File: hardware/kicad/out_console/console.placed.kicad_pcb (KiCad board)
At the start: 2 copper layers, 99.5 x 99.5 mm, 65 parts, among them J1 RaspberryPi_Pico_SMD_HandSold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, J10 JST_XH_B2B-XH-A_1x02_P2.50mm_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, J11 JST_XH_B2B-XH-A_1x02_P2.50mm_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, J12 JST_XH_B2B-XH-A_1x02_P2.50mm_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, J13 JST_XH_B2B-XH-A_1x02_P2.50mm_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, J14 JST_XH_B2B-XH-A_1x02_P2.50mm_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, J15 JST_XH_B2B-XH-A_1x02_P2.50mm_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, J16 JST_XH_B2B-XH-A_1x02_P2.50mm_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, J17 JST_XH_B2B-XH-A_1x02_P2.50mm_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, J18 JST_XH_B2B-XH-A_1x02_P2.50mm_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, J19 JST_XH_B2B-XH-A_1x02_P2.50mm_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, J2 IDC-Header_2x20_P2.54mm_Verti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, J20 JST_XH_B4B-XH-A_1x04_P2.50mm_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, J21 JST_XH_B4B-XH-A_1x04_P2.50mm_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, J22 PinHeader_2x03_P2.54mm_Vertic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, J23 JST_XH_B3B-XH-A_1x03_P2.50mm_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, J24 JST_VH_B3P-VH_1x03_P3.96mm_Ve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, J3 JST_VH_B2P-VH_1x02_P3.96mm_Ve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, J4 JST_XH_B3B-XH-A_1x03_P2.50mm_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, J5 JST_XH_B2B-XH-A_1x02_P2.50mm_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, J6 JST_XH_B4B-XH-A_1x04_P2.50mm_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, J8 JST_XH_B2B-XH-A_1x02_P2.50mm_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, J9 JST_XH_B2B-XH-A_1x02_P2.50mm_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, U1 DIP-14_W7.62mm, U2 DIP-6_W7.62mm

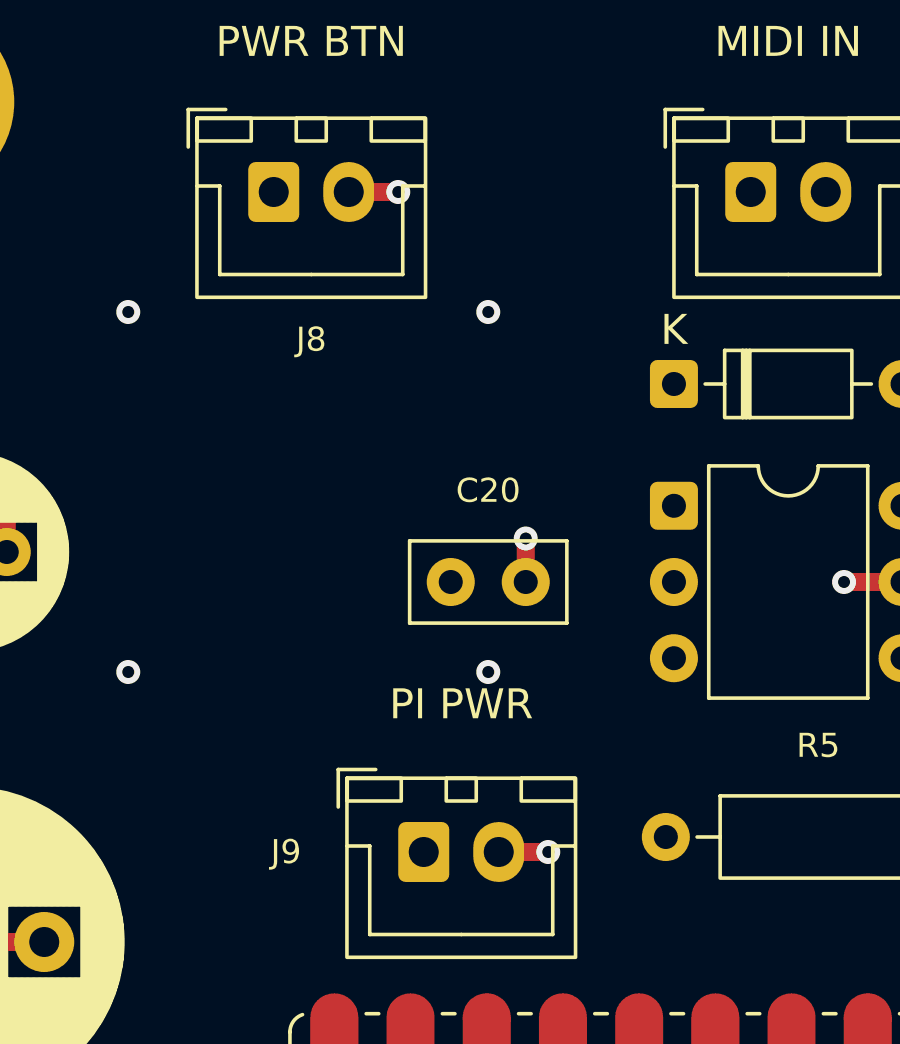
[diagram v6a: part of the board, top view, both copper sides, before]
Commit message: fix(hardware): the power button lead is a floating pair, not signal and GND (#1062)
J8 and J9 were wired PWR_BTN + GND. Nothing on the board reads the button,
and a lead fitted to the Pi 5's J2 pads the wrong way round held the button
pad at ground, which the Pi reads as a button held down. They are now wired
pin to pin (PWR_BTN, PWR_BTN_RET) with neither touching GND, so the lead
works either way round. PWR_BTN gates the floating pair; rerouted, DRC clean.
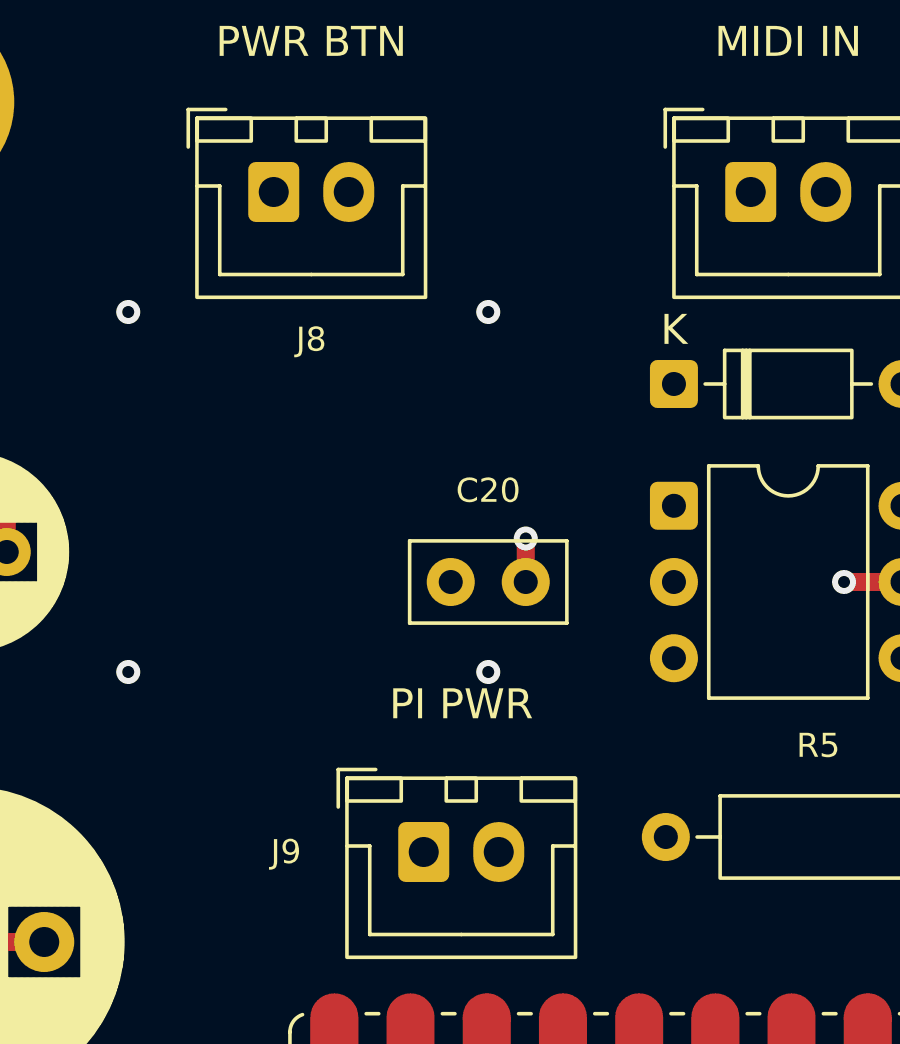
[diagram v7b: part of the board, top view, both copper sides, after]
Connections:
- J8 pad 2: GND -> PWR_BTN_RET
- J9 pad 2: GND -> PWR_BTN_RET
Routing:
- net GND: track 116.0 -> 112.7 mm, vias 73 -> 71

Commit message: fix(hardware): drop the MIDI IN legend from the console silkscreen (#1062)
Owner call: the bottom strip reads better with the title alone. Removed in the
generator rather than by hand, so it does not come back on the next run; the
board was re-placed, re-routed and re-exported with it gone. DRC 0 violations,
0 unconnected, fab checks pass.
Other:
- board text removed: "MIDI IN: ISOLATED"
